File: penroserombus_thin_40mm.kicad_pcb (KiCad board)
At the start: 2 copper layers, 72.4 x 23.5 mm, 13 parts, among them J1 Conn_01x03_Female, J2 Conn_01x03_Female, J3 Conn_01x03_Male, J4 Conn_01x03_Male, SW1 SW_DPDT_x2

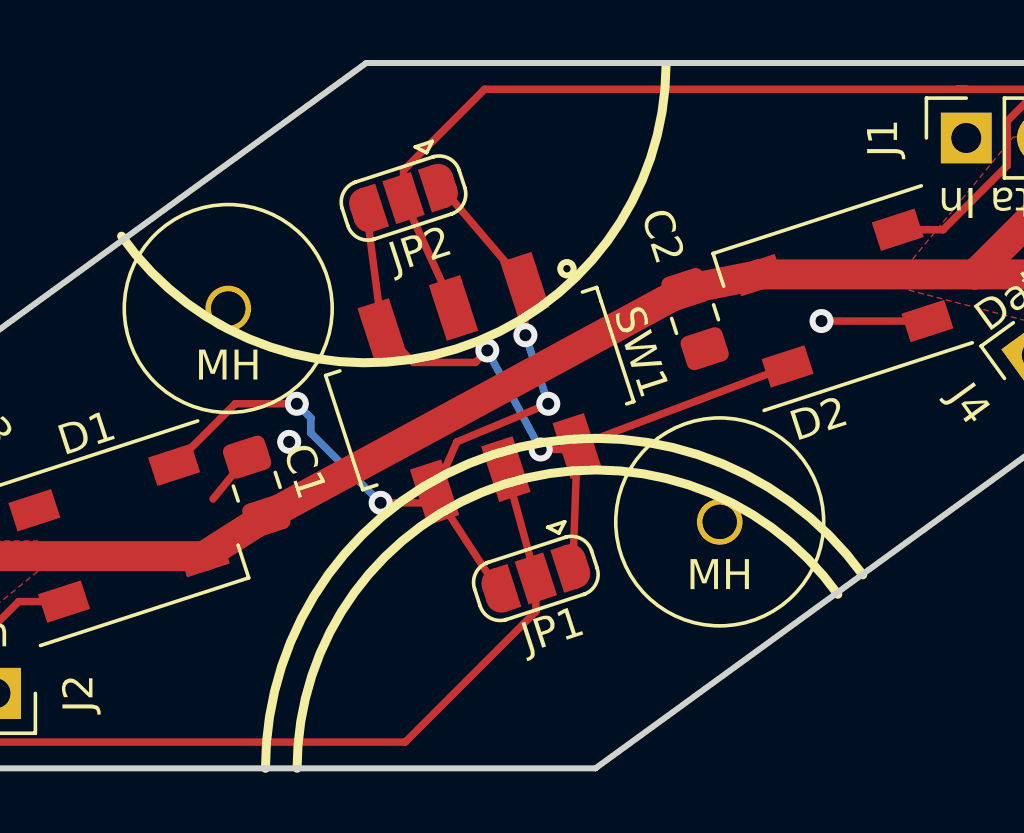
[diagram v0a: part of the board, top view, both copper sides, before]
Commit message: added more mounting holes and generated gerbers
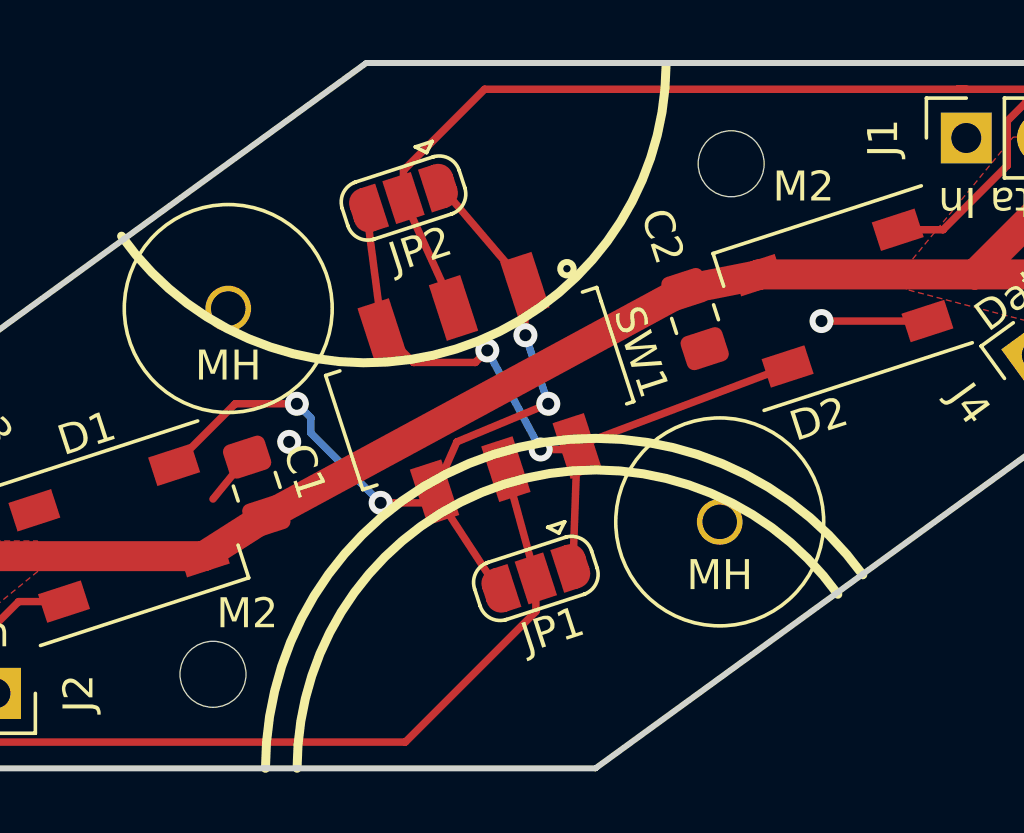
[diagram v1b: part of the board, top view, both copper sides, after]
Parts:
- added M2: MountingHole_2.2mm_M2_ISO7380, MountingHole:MountingHole_2.2mm_M2_ISO7380, F.Cu at (146.1, 81.9)
- added M2: MountingHole_2.2mm_M2_ISO7380, MountingHole:MountingHole_2.2mm_M2_ISO7380, F.Cu at (163.3, 64.9)
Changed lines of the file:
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@@
     (tracks 82)
     (zones 0)
-    (modules 13)
+    (modules 15)
     (nets 9)
   )
@@
     (add_net VCC)
   )
+  (module MountingHole:MountingHole_2.2mm_M2_ISO7380 (layer F.Cu)
+    (at 146.05 81.915)
+    (descr "Mounting Hole 2.2mm, no annular, M2, ISO7380")
+    (tags "mounting hole 2.2mm no annular m2 iso7380")
+    (attr virtual)
+    (fp_text reference M2 (at 1.143 -2.032) (layer F.SilkS)
+      (effects (font (size 1 1) (thickness 0.15)))
+    )
+    (fp_text value MountingHole_2.2mm_M2_ISO7380 (at 0 2.75) (layer F.Fab)
+      (effects (font (size 1 1) (thickness 0.15)))
+    )
+    (fp_circle (center 0 0) (end 2 0) (layer F.CrtYd) (width 0.05))
+    (fp_circle (center 0 0) (end 1.75 0) (layer Cmts.User) (width 0.15))
+    (fp_text user %R (at 0.3 0) (layer F.Fab)
+      (effects (font (size 1 1) (thickness 0.15)))
+    )
+    (pad 1 np_thru_hole circle (at 0 0) (size 2.2 2.2) (drill 2.2) (layers *.Cu *.Mask))
+  )
+  (module MountingHole:MountingHole_2.2mm_M2_ISO7380 (layer F.Cu)
+    (at 163.322 64.897)
+    (descr "Mounting Hole 2.2mm, no annular, M2, ISO7380")
+    (tags "mounting hole 2.2mm no annular m2 iso7380")
+    (attr virtual)
+    (fp_text reference M2 (at 2.413 0.762) (layer F.SilkS)
+      (effects (font (size 1 1) (thickness 0.15)))
+    )
+    (fp_text value MountingHole_2.2mm_M2_ISO7380 (at 0 2.75) (layer F.Fab)
+      (effects (font (size 1 1) (thickness 0.15)))
+    )
+    (fp_circle (center 0 0) (end 2 0) (layer F.CrtYd) (width 0.05))
+    (fp_circle (center 0 0) (end 1.75 0) (layer Cmts.User) (width 0.15))
+    (fp_text user %R (at 0.3 0) (layer F.Fab)
+      (effects (font (size 1 1) (thickness 0.15)))
+    )
+    (pad 1 np_thru_hole circle (at 0 0) (size 2.2 2.2) (drill 2.2) (layers *.Cu *.Mask))
+  )
   (module penroserombus:Pushpin_mountinghole (layer F.Cu)
     (at 162.941 76.835)
@@
     (pad "" np_thru_hole circle (at 0 0) (size 1.524 1.524) (drill 1.15) (layers *.Cu *.Mask))
   )
-  (module Connector_PinSocket_2.54mm:PinSocket_1x03_P2.54mm_Vertical (layer F.Cu)
+  (module Connector_PinSocket_2.54mm:PinSocket_1x03_P2.54mm_Vertical locked (layer F.Cu)
     (at 136.448848 75.316838 306)
     (descr "Through hole straight socket strip, 1x03, 2.54mm pitch, single row (from Kicad 4.0.7), script generated")
@@
     )
   )
-  (module Connector_PinSocket_2.54mm:PinSocket_1x03_P2.54mm_Vertical (layer F.Cu)
+  (module Connector_PinSocket_2.54mm:PinSocket_1x03_P2.54mm_Vertical locked (layer F.Cu)
     (at 171.159724 64.03859 90)
     (descr "Through hole straight socket strip, 1x03, 2.54mm pitch, single row (from Kicad 4.0.7), script generated")
@@
     )
   )
-  (module Connector_PinSocket_2.54mm:PinSocket_1x03_P2.54mm_Vertical (layer F.Cu)
+  (module Connector_PinSocket_2.54mm:PinSocket_1x03_P2.54mm_Vertical locked (layer F.Cu)
     (at 138.799045 82.55 270)
     (descr "Through hole straight socket strip, 1x03, 2.54mm pitch, single row (from Kicad 4.0.7), script generated")
@@
     )
   )
-  (module Connector_PinSocket_2.54mm:PinSocket_1x03_P2.54mm_Vertical (layer F.Cu)
+  (module Connector_PinSocket_2.54mm:PinSocket_1x03_P2.54mm_Vertical locked (layer F.Cu)
     (at 173.509921 71.271753 126)
     (descr "Through hole straight socket strip, 1x03, 2.54mm pitch, single row (from Kicad 4.0.7), script generated")

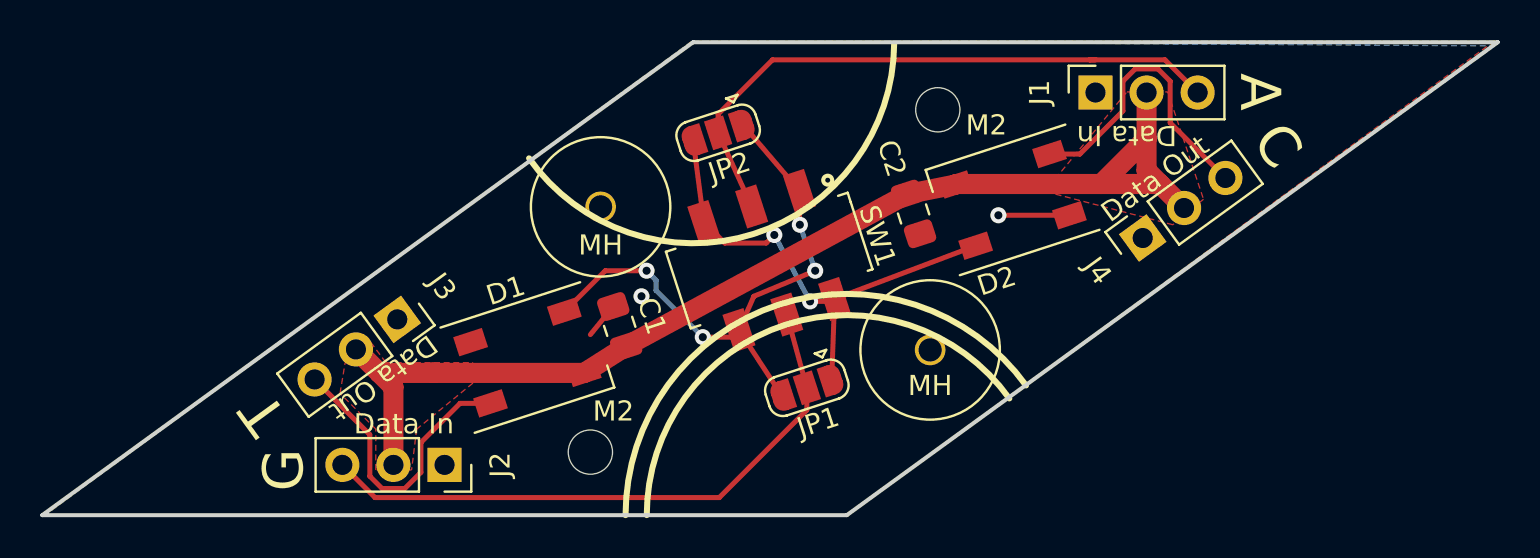
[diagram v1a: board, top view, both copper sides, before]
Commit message: changed out 5050 leds for 2020 led
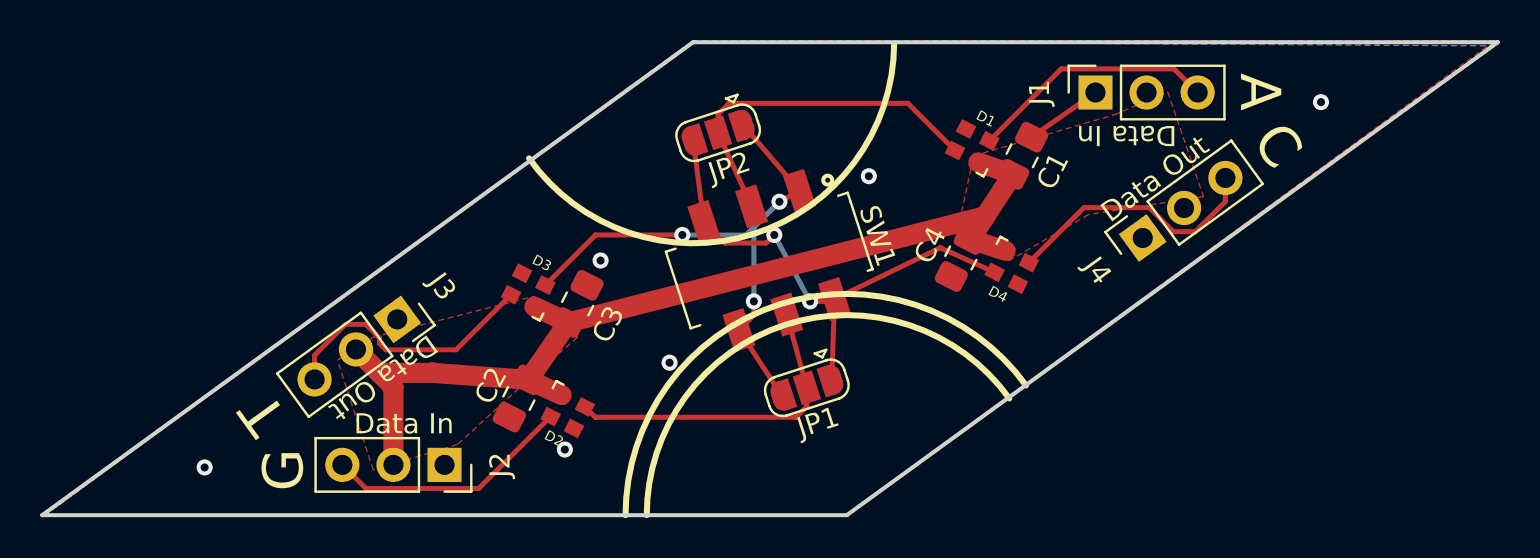
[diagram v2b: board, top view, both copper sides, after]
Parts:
- removed M2 (x2): MountingHole_2.2mm_M2_ISO7380, MountingHole:MountingHole_2.2mm_M2_ISO7380
- removed MH (x2): Pushpin_mountinghole, penroserombus:Pushpin_mountinghole
- added C3: C, Capacitor_SMD:C_0805_2012Metric_Pad1.18x1.45mm_HandSolder, F.Cu at (145.4, 74.5)
- added C4: C, Capacitor_SMD:C_0805_2012Metric_Pad1.18x1.45mm_HandSolder, F.Cu at (164.5, 72.3)
- added D3: SK6812, penroserombus:SK6812_2020_LED, F.Cu at (143.0, 73.9)
- added D4: SK6812, penroserombus:SK6812_2020_LED, F.Cu at (167.0, 72.7)
- D1, D2: footprint LED_SMD:LED_SK6812_PLCC4_5.0x5.0mm_P3.2mm -> penroserombus:SK6812_2020_LED
- moved D2 24.5 mm to (144.9, 79.9), turned to 153 degrees
- moved D1 24.5 mm to (165.0, 66.7), turned to 333 degrees
- moved C1 21.7 mm to (167.5, 67.2), turned to 243 degrees
- moved C2 21.7 mm to (142.5, 79.2), turned to 63 degrees
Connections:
- J1 pad 3: Net-(J1-Pad3) -> Net-(D1-Pad2)
- J2 pad 3: Net-(J2-Pad3) -> Net-(D2-Pad2)
- J3 pad 3: Net-(D1-Pad4) -> Net-(D3-Pad4)
- J4 pad 3: Net-(D2-Pad4) -> Net-(D4-Pad4)
- JP1 pad 1: Net-(D2-Pad2) -> Net-(D4-Pad2)
- JP1 pad 2: Net-(J2-Pad3) -> Net-(D2-Pad4)
- JP1 pad 3: Net-(D1-Pad2) -> Net-(D3-Pad2)
- JP2 pad 1: Net-(D1-Pad2) -> Net-(D3-Pad2)
- JP2 pad 2: Net-(J1-Pad3) -> Net-(D1-Pad4)
- JP2 pad 3: Net-(D2-Pad2) -> Net-(D4-Pad2)
- SW1 pad 1: Net-(D1-Pad2) -> Net-(D3-Pad2)
- SW1 pad 2: Net-(J1-Pad3) -> Net-(D1-Pad4)
- SW1 pad 3: Net-(D2-Pad2) -> Net-(D4-Pad2)
- SW1 pad 4: Net-(D2-Pad2) -> Net-(D4-Pad2)
- SW1 pad 5: Net-(J2-Pad3) -> Net-(D2-Pad4)
- SW1 pad 6: Net-(D1-Pad2) -> Net-(D3-Pad2)
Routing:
- net Net-(J1-Pad3): track 30.9 -> 0.00 mm
- net Net-(J2-Pad3): track 30.4 -> 0.00 mm
- net Net-(D3-Pad2): track 0.00 -> 28.6 mm, vias 0 -> 3
- net Net-(D4-Pad2): track 0.00 -> 26.2 mm, vias 0 -> 2
- net Net-(D1-Pad2): track 29.2 -> 12.3 mm, vias 4 -> 0
- net Net-(D3-Pad4): track 0.00 -> 13.4 mm
- net Net-(D4-Pad4): track 0.00 -> 13.2 mm
- net Net-(D2-Pad2): track 24.9 -> 12.3 mm, vias 2 -> 0
- net VCC: track 57.4 -> 50.0 mm
- net Net-(D1-Pad4): track 14.9 -> 17.9 mm
- net GND: track 5.37 -> 3.87 mm, vias 2 -> 6
- net Net-(D2-Pad4): track 14.8 -> 16.2 mm
